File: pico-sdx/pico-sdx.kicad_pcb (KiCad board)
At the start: 2 copper layers, 76.7 x 64.5 mm, 100 parts, among them J1 AudioJack3, J2 AudioJack3, J3 Screw_Terminal_01x02, J4 Conn_Coaxial, J5 Conn_Coaxial, T1 T-622, T2 Transformer_SP_1S, U1 74HC74, U2 4066, U3 OPA2350, U4 LM321, U5 74HC74, U6 4066, U7 OPA1602, U8 uA7805, U9 uA7805

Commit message: update clock module footprint
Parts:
- moved J3 134.4 mm to (170.1, 92.3)
- moved C39 131.6 mm to (174.1, 77.9)
- moved C45 131.6 mm to (174.1, 82.9)
- moved C40 131.6 mm to (169.3, 66.3)
- moved C41 131.6 mm to (169.3, 69.5)
- moved C42 131.6 mm to (174.1, 80.4)
- moved C43 131.6 mm to (169.3, 72.6)
- moved C44 131.6 mm to (169.3, 75.8)
- moved U8 131.6 mm to (175.3, 68.7)
- moved U9 131.6 mm to (175.3, 74.6)
- moved C35 79.3 mm to (141.1, 28.5)
- moved R27 79.3 mm to (160.0, 28.4)
- moved R30 79.3 mm to (161.4, 23.0)
- moved RV2 79.3 mm to (174.4, 24.4)
- moved RV3 79.3 mm to (163.9, 19.4)
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
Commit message: add documentation and RaspberryPi Pico
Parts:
- added U11: RaspberryPi_Pico, Module_RaspberryPi_Pico:RaspberryPi_Pico_Common, F.Cu at (270.6, 101.0)
- C35, C36: moved to B.Cu
- C40: value 1µF -> 100nF; footprint Capacitor_Tantalum_SMD:CP_EIA-3216-18_Kemet-A -> Capacitor_SMD:C_0603_1608Metric
- C42: value 100nF -> 1µF; footprint Capacitor_SMD:C_0603_1608Metric -> Capacitor_Tantalum_SMD:CP_EIA-3216-18_Kemet-A
- moved C19 131.7 mm to (146.8, -16.0)
- moved C20 131.7 mm to (146.8, -17.5)
- moved R25 131.7 mm to (149.8, -19.0)
- moved R26 131.7 mm to (146.8, -19.0)
- moved R28 131.7 mm to (147.3, -21.6)
- moved R29 131.7 mm to (149.3, -21.6)
- moved C13 108.8 mm to (47.1, -32.0)
- moved C14 108.8 mm to (52.6, -31.0)
- moved C34 108.8 mm to (42.5, -29.9)
- moved R15 108.8 mm to (48.6, -32.0)
- moved R16 108.8 mm to (47.1, -28.9)
- moved U4 108.8 mm to (42.8, -32.8)
- moved C35 89.3 mm to (53.3, 45.0), turned to 0 degrees
- moved R27 82.6 mm to (92.0, -18.4)
- moved R30 82.6 mm to (93.4, -23.8)
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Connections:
- net /Oscillator/CLK0 renamed /downconverter/RX_LO
- net /Oscillator/CLK1 renamed /upconverter/TX_LO
- C41 pad 1: +5VA -> +12V
- C43 pad 1: +12V -> +5VD
- C44 pad 1: +5VD -> +5VA
- U10 pad 3: /Oscillator/CLK2 -> unconnected-(U10-CLK2-Pad3)
- U8 pad 3: +5VA -> +5VD
- U9 pad 3: +5VD -> +5VA
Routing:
- net +5VD: track 21.0 -> 25.2 mm
- net Net-(C24-Pad2): track 4.24 -> 2.27 mm
- net Net-(C21-Pad2): track 4.24 -> 2.52 mm

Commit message: routed with filter relays without PA
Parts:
- added C46: 1µF, Capacitor_SMD:C_0603_1608Metric, F.Cu at (101.9, 42.7)
- added C50: 1µF, Capacitor_SMD:C_0603_1608Metric, F.Cu at (101.9, 49.3)
- added D1: D, Diode_SMD:D_SOD-128, B.Cu at (28.8, 68.4)
- added D2: D, Diode_SMD:D_SOD-128, B.Cu at (104.7, 49.7)
- added D3: D, Diode_SMD:D_SOD-128, B.Cu at (28.7, 31.5)
- added D4: D, Diode_SMD:D_SOD-128, B.Cu at (41.7, 31.5)
- added D5: D, Diode_SMD:D_SOD-128, B.Cu at (54.7, 31.5)
- added D6: D, Diode_SMD:D_SOD-128, B.Cu at (67.7, 31.5)
- added D7: D, Diode_SMD:D_SOD-128, B.Cu at (80.7, 31.5)
- added D8: D, Diode_SMD:D_SOD-128, B.Cu at (93.7, 31.5)
- added D9: D, Diode_SMD:D_SOD-128, B.Cu at (107.2, 30.5)
- added J1: Antenna, Connector_Coaxial:SMA_Amphenol_132289_EdgeMount, F.Cu at (18.6, 77.9)
- added J2: RX, Connector_Coaxial:SMA_Amphenol_132289_EdgeMount, F.Cu at (18.6, 65.9)
- added J3: TX, Connector_Coaxial:SMA_Amphenol_132289_EdgeMount, F.Cu at (18.6, 89.9)
- added JP1: Jumper_3_Open, Connector_PinHeader_1.27mm:PinHeader_1x03_P1.27mm_Vertical, F.Cu at (24.2, 88.7)
- added JP2: Jumper_3_Open, Connector_PinHeader_1.27mm:PinHeader_1x03_P1.27mm_Vertical, F.Cu at (28.0, 88.7)
- added K1: G6K-2, Relay_THT:Relay_DPDT_Omron_G6K-2P, F.Cu at (108.0, 52.2)
- added K2: G6K-2, Relay_THT:Relay_DPDT_Omron_G6K-2P, F.Cu at (26.2, 71.7)
- added K3: G6K-2, Relay_THT:Relay_DPDT_Omron_G6K-2P, F.Cu at (25.9, 28.9)
- added K4: G6K-2, Relay_THT:Relay_DPDT_Omron_G6K-2P, F.Cu at (38.9, 28.9)
- added K5: G6K-2, Relay_THT:Relay_DPDT_Omron_G6K-2P, F.Cu at (51.9, 28.9)
- added K6: G6K-2, Relay_THT:Relay_DPDT_Omron_G6K-2P, F.Cu at (64.9, 28.9)
- added K7: G6K-2, Relay_THT:Relay_DPDT_Omron_G6K-2P, F.Cu at (77.9, 28.9)
- added K8: G6K-2, Relay_THT:Relay_DPDT_Omron_G6K-2P, F.Cu at (90.9, 28.9)
- added K9: G6K-2, Relay_THT:Relay_DPDT_Omron_G6K-2P, F.Cu at (103.9, 28.9)
- added L1: 27µH, Inductor_SMD:L_Bourns_SRR1208_12.7x12.7mm, F.Cu at (93.8, 46.0)
- added R36: 1.8R, Resistor_SMD:R_0603_1608Metric, F.Cu at (101.2, 40.4)
- added TP1: RX_LO, TestPoint:TestPoint_Loop_D1.80mm_Drill1.0mm_Beaded, F.Cu at (125.2, 49.9)
- added TP10: TestPoint, TestPoint:TestPoint_Loop_D1.80mm_Drill1.0mm_Beaded, F.Cu at (167.1, 46.4)
- added TP11: TestPoint, TestPoint:TestPoint_Loop_D1.80mm_Drill1.0mm_Beaded, F.Cu at (148.2, 36.9)
- added TP12: TestPoint, TestPoint:TestPoint_Loop_D1.80mm_Drill1.0mm_Beaded, F.Cu at (140.2, 48.7)
- added TP2: TX_LO, TestPoint:TestPoint_Loop_D1.80mm_Drill1.0mm_Beaded, F.Cu at (129.2, 48.9)
- added TP3: RX_TR_Midpoint, TestPoint:TestPoint_Loop_D1.80mm_Drill1.0mm_Beaded, F.Cu at (112.2, 76.9)
- added TP4: RX_OPAMP_Midpoint, TestPoint:TestPoint_Loop_D1.80mm_Drill1.0mm_Beaded, F.Cu at (144.8, 63.8)
- added TP5: TestPoint, TestPoint:TestPoint_Loop_D1.80mm_Drill1.0mm_Beaded, F.Cu at (152.1, 36.7)
- added TP6: TestPoint, TestPoint:TestPoint_Loop_D1.80mm_Drill1.0mm_Beaded, F.Cu at (147.4, 22.6)
- added TP7: TestPoint, TestPoint:TestPoint_Loop_D1.80mm_Drill1.0mm_Beaded, F.Cu at (167.1, 62.7)
- added TP8: TestPoint, TestPoint:TestPoint_Loop_D1.80mm_Drill1.0mm_Beaded, F.Cu at (135.6, 39.5)
- added TP9: TestPoint, TestPoint:TestPoint_Loop_D1.80mm_Drill1.0mm_Beaded, F.Cu at (139.7, 39.5)
- added U1: MAX4820xUP, Package_SO:HTSSOP-20-1EP_4.4x6.5mm_P0.65mm_EP2.85x4mm, B.Cu at (94.5, 66.9)
- added U13: HMC589A, Package_TO_SOT_SMD:SOT-89-3, F.Cu at (103.3, 46.0)
- added X1: 40 m, pico-sdx:Filter Module, F.Cu at (22.2, 40.9)
- added X2: 30 m, pico-sdx:Filter Module, F.Cu at (35.2, 40.9)
- added X3: 20 m, pico-sdx:Filter Module, F.Cu at (48.2, 40.9)
- added X4: 17 m, pico-sdx:Filter Module, F.Cu at (61.2, 40.9)
- added X5: 15 m, pico-sdx:Filter Module, F.Cu at (74.2, 40.9)
- added X6: 12 m, pico-sdx:Filter Module, F.Cu at (87.2, 40.9)
- added X7: 10 m, pico-sdx:Filter Module, F.Cu at (100.2, 40.9)
- C14: renamed from C36; moved to F.Cu
- C42: renamed from C35; moved to F.Cu
- J4, J5: footprint Connector_Coaxial:SMA_Amphenol_132289_EdgeMount -> Connector_Coaxial:SMA_Amphenol_132291_Vertical
- J8: renamed from J3; value Screw_Terminal_01x02 -> Barrel_Jack_Switch; footprint TerminalBlock:TerminalBlock_Wuerth_691311400102_P7.62mm -> Connector_BarrelJack:BarrelJack_Wuerth_6941xx301002
- U6: renamed from U1; moved to F.Cu
- U9: renamed from U5; moved to F.Cu
- moved C22 127.6 mm to (155.2, 63.4), turned to 90 degrees
- moved C19 126.4 mm to (149.2, 64.8)
- moved R13 126.4 mm to (149.2, 61.5)
- moved R14 126.4 mm to (147.5, 64.8)
- moved C31 125.6 mm to (154.7, 42.3)
- moved C32 125.6 mm to (149.1, 41.4)
- moved C38 125.6 mm to (144.5, 43.4)
- moved R25 125.6 mm to (149.1, 44.4)
- moved R26 125.6 mm to (150.6, 41.4)
- moved U11 125.6 mm to (144.8, 40.5)
- moved J8 122.1 mm to (29.6, 100.7), turned to -90 degrees
- moved U2 121.7 mm to (149.1, 95.1), turned to -90 degrees
- moved RV2 113.2 mm to (170.6, 57.7)
- moved R29 111.6 mm to (168.1, 59.0)
- moved R33 105.4 mm to (168.1, 54.5)
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- renumbered C39 to C1, C4 to C10, C3 to C11, C5 to C12, C6 to C13, C7 to C15, C8 to C16, C37 to C17, C9 to C18, C11 to C19, C40 to C2, C38 to C20, C10 to C21, C12 to C22, C15 to C23, C16 to C24, C17 to C25, C18 to C26, C21 to C27, C22 to C28, C23 to C29, C41 to C3, C24 to C30, C14 to C31, C13 to C32, C25 to C33, C26 to C34, C27 to C35, C28 to C36, C31 to C37, C34 to C38, C30 to C39, C42 to C4, C33 to C40, C29 to C41, C20 to C43, C32 to C44, C19 to C45, C43 to C5, C44 to C6, C45 to C7, C1 to C8, C2 to C9, J1 to J6, J2 to J7, R17 to R15, R18 to R16, R21 to R17, R22 to R18, R20 to R19, R19 to R20, R32 to R21, R33 to R22, R34 to R23, R35 to R24, R16 to R25, R15 to R26, R23 to R27, R24 to R28, R30 to R29, R28 to R30, R25 to R31, R26 to R32, R27 to R33, R29 to R34, R31 to R35, R6 to R5, R5 to R6, RV3 to RV2, RV2 to RV3, U7 to U10, U4 to U11, U6 to U12, U11 to U2, U10 to U3, U8 to U4, U9 to U5, U2 to U7, U3 to U8
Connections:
- net /downconverter/2.5V_OPAMP renamed /Downconverter/2.5V_OPAMP
- net /downconverter/2.5V_TR renamed /Downconverter/2.5V_TR
- net /downconverter/CLK_I renamed /Downconverter/CLK_I
- net /downconverter/CLK_Q renamed /Downconverter/CLK_Q
- net /downconverter/RX_I renamed /Downconverter/RX_I
- net /downconverter/RX_IN renamed /Downconverter/RX_IN
- net /downconverter/RX_Q renamed /Downconverter/RX_Q
- net /downconverter/~{CLK_I} renamed /Downconverter/~{CLK_I}
- net /downconverter/~{CLK_Q} renamed /Downconverter/~{CLK_Q}
- net /upconverter/2.5V renamed /Upconverter/2.5V
- net /upconverter/BIAS renamed /Upconverter/BIAS
- net /upconverter/BIAS_I renamed /Upconverter/BIAS_I
- net /upconverter/BIAS_Q renamed /Upconverter/BIAS_Q
- net /upconverter/CLK_I renamed /Upconverter/CLK_I
- net /upconverter/CLK_Q renamed /Upconverter/CLK_Q
- net /upconverter/TX_I renamed /Upconverter/TX_I
- net /upconverter/TX_OUT renamed /Upconverter/TX_OUT
- net /upconverter/TX_Q renamed /Upconverter/TX_Q
- net /upconverter/~{BIAS_I} renamed /Upconverter/~{BIAS_I}
- net /upconverter/~{BIAS_Q} renamed /Upconverter/~{BIAS_Q}
- net /upconverter/~{CLK_I} renamed /Upconverter/~{CLK_I}
- net /upconverter/~{CLK_Q} renamed /Upconverter/~{CLK_Q}
- R33 pad 2: Net-(R27-Pad2) (its old number) -> Net-(R33-Pad2)
- RV2 pad 1: GND -> Net-(R33-Pad2)
- RV2 pad 3: Net-(R27-Pad2) (its old number) -> GND
- RV3 pad 1: Net-(R27-Pad2) (its old number) -> GND
- RV3 pad 3: GND -> Net-(R33-Pad2)
- U2 pad 19: unconnected-(U11-GPIO14-Pad19) -> SDA
- U2 pad 20: unconnected-(U11-GPIO15-Pad20) -> SCL
- U2 pad 21: unconnected-(U11-GPIO16-Pad21) -> MISO
- U2 pad 22: unconnected-(U11-GPIO17-Pad22) -> ~{CS}
- U2 pad 24: unconnected-(U11-GPIO18-Pad24) -> SCLK
- U2 pad 25: SDA -> MOSI
- U2 pad 26: SCL -> ~{RESET}
- U2 pad 39: unconnected-(U11-VSYS-Pad39) -> +5VD
- U3 pad 1: /downconverter/RX_LO -> +5VD
- U3 pad 2: /upconverter/TX_LO -> GND
- U3 pad 3: unconnected-(U10-CLK2-Pad3) -> SDA
- U3 pad 5: SDA -> unconnected-(U3-CLK2-Pad5)
- U3 pad 6: GND -> RX_LO
- U3 pad 7: (no net) -> TX_LO
- U6 pad 11: /downconverter/RX_LO -> RX_LO
- U6 pad 3: /downconverter/RX_LO -> RX_LO
- U9 pad 11: /upconverter/TX_LO -> TX_LO
- U9 pad 3: /upconverter/TX_LO -> TX_LO
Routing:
- net +5VD: track 25.2 -> 304.7 mm, vias 0 -> 6
- net +5VA: track 5.15 -> 263.4 mm, vias 0 -> 8
- net /Bandpass Filter/RF in: track 0.00 -> 123.2 mm
- net /Bandpass Filter/RF out: track 0.00 -> 122.7 mm
- net /PA/TX in: track 0.00 -> 119.4 mm
- net Net-(J2-In): track 0.00 -> 113.2 mm
- net +12V: track 0.00 -> 112.3 mm
- net TX~{RX}: track 0.00 -> 110.7 mm, vias 0 -> 2
- net 40 m: track 0.00 -> 102.2 mm
- net 30 m: track 0.00 -> 89.7 mm
- net 20 m: track 0.00 -> 76.4 mm
- net ~{RESET}: track 0.00 -> 75.1 mm
- net MOSI: track 0.00 -> 73.7 mm
- net SCLK: track 0.00 -> 71.8 mm
- net ~{CS}: track 0.00 -> 66.4 mm, vias 0 -> 1
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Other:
- board size 76.7 x 64.5 mm -> 160 x 100 mm
- board text added: "{ "ViaStitching": "0.2", "stitch_zone_0": { "HSpacing": "1", "VSpacing": "1", "Clearance": "0.2", "Randomize": false } }"

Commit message: add active lowpass filter in upconverter branch
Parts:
- added C51: 100nF, Capacitor_SMD:C_0603_1608Metric, F.Cu at (140.7, 26.8)
- added C52: 100pF, Capacitor_SMD:C_1206_3216Metric, F.Cu at (151.4, 34.5)
- added C53: 100pF, Capacitor_SMD:C_1206_3216Metric, F.Cu at (151.4, 26.6)
- added R37: 10k, Resistor_SMD:R_0603_1608Metric, F.Cu at (153.4, 25.8)
- added R38: 10k, Resistor_SMD:R_0603_1608Metric, F.Cu at (153.4, 32.4)
- added R39: 7.5k, Resistor_SMD:R_0603_1608Metric, F.Cu at (153.4, 29.1)
- added R40: 7.5k, Resistor_SMD:R_0603_1608Metric, F.Cu at (153.4, 22.5)
- added U14: OPA1602, Package_SO:SOIC-8_3.9x4.9mm_P1.27mm, F.Cu at (146.3, 25.2)
- moved TP6 24.3 mm to (164.8, 39.5)
- moved C44 12.3 mm to (143.2, 35.9), turned to 180 degrees
- moved TP5 8.12 mm to (159.7, 39.5)
- moved R16 7.97 mm to (158.5, 21.5)
- moved C25 7.88 mm to (156.7, 34.7), turned to 180 degrees
- moved C26 7.19 mm to (155.4, 23.0), turned to 90 degrees
- moved R18 5.21 mm to (146.8, 21.6), turned to 180 degrees
- moved U10 4.61 mm to (146.3, 32.3), turned to 180 degrees
- moved R15 4.44 mm to (158.5, 32.7)
- moved C23 4.06 mm to (155.9, 31.4)
- moved C24 4.06 mm to (155.9, 27.3)
- moved R17 3.18 mm to (146.8, 28.7), turned to 180 degrees
- moved C29 2.84 mm to (139.4, 28.9), turned to 180 degrees
- moved R19 2.16 mm to (141.7, 32.3), turned to -90 degrees
- moved R20 1.61 mm to (141.6, 24.0), turned to -90 degrees
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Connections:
- C27 pad 1: Net-(C25-Pad2) -> Net-(C27-Pad1)
- C29 pad 1: Net-(C26-Pad2) -> Net-(C29-Pad1)
- R17 pad 1: Net-(C25-Pad2) -> Net-(C27-Pad1)
- R17 pad 2: Net-(U10A--) -> Net-(U10B--)
- R18 pad 1: Net-(C26-Pad2) -> Net-(C29-Pad1)
- R18 pad 2: Net-(U10B--) -> Net-(U14B--)
- R19 pad 1: Net-(U10A--) -> Net-(U10B--)
- R20 pad 1: Net-(U10B--) -> Net-(U14B--)
- U10 pad 1: Net-(C28-Pad1) -> Net-(C27-Pad1)
- U10 pad 7: Net-(C30-Pad1) -> Net-(C28-Pad1)
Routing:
- net /Upconverter/2.5V: track 24.5 -> 53.2 mm, vias 2 -> 4
- net Net-(C27-Pad1): track 0.00 -> 25.7 mm
- net Net-(C29-Pad1): track 0.00 -> 20.6 mm
- net Net-(C24-Pad1): track 9.13 -> 26.0 mm, vias 0 -> 1
- net Net-(C26-Pad2): track 12.4 -> 2.09 mm
- net Net-(C25-Pad2): track 17.2 -> 7.14 mm
- net GND: track 50.9 -> 60.6 mm, vias 24 -> 17
- net Net-(U14B--): track 0.00 -> 7.10 mm
- net Net-(U14A--): track 0.00 -> 6.63 mm
- net /Upconverter/~{BIAS_Q}: track 56.2 -> 62.6 mm
- net Net-(C30-Pad1): track 12.0 -> 6.56 mm
- net /Upconverter/TX_Q: track 18.3 -> 13.0 mm
- net Net-(R15-Pad1): track 20.8 -> 16.0 mm
- net +5VA: track 263.4 -> 265.8 mm, vias 8 -> 9
- net Net-(C29-Pad2): track 4.37 -> 2.62 mm
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
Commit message: modular design
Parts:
- removed D1, D2, D3, D4, D5, D6, D7, D8, D9: D, Diode_SMD:D_SOD-128
- removed J1: Antenna, Connector_Coaxial:SMA_Amphenol_132289_EdgeMount
- removed J2: RX, Connector_Coaxial:SMA_Amphenol_132289_EdgeMount
- removed J3: TX, Connector_Coaxial:SMA_Amphenol_132289_EdgeMount
- removed JP1, JP2: Jumper_3_Open, Connector_PinHeader_1.27mm:PinHeader_1x03_P1.27mm_Vertical
- removed K1, K2, K3, K4, K5, K6, K7, K8, K9: G6K-2, Relay_THT:Relay_DPDT_Omron_G6K-2P
- removed TP1: RX_LO, TestPoint:TestPoint_Loop_D1.80mm_Drill1.0mm_Beaded
- removed TP2: TX_LO, TestPoint:TestPoint_Loop_D1.80mm_Drill1.0mm_Beaded
- removed U1: MAX4820xUP, Package_SO:HTSSOP-20-1EP_4.4x6.5mm_P0.65mm_EP2.85x4mm
- removed U2: RaspberryPi_Pico, Module_RaspberryPi_Pico:RaspberryPi_Pico_Common
- removed U4: uA7805, Package_TO_SOT_THT:TO-220-3_Vertical
- removed X1: 40 m, pico-sdx:Filter Module
- removed X2: 30 m, pico-sdx:Filter Module
- removed X3: 20 m, pico-sdx:Filter Module
- removed X4: 17 m, pico-sdx:Filter Module
- removed X5: 15 m, pico-sdx:Filter Module
- removed X6: 12 m, pico-sdx:Filter Module
- removed X7: 10 m, pico-sdx:Filter Module
- added PMOD1: PMOD-Device-x2-Type-2A-Expanded-SPI, pmod-conn_6x2:pmod_pin_array_6x2, F.Cu at (40.0, 72.3)
- added U17: TLE4284 DV33, Package_TO_SOT_SMD:TO-252-3_TabPin2, F.Cu at (92.3, 88.7)
- added X8: TCXO-14, Oscillator:Oscillator_DIP-14, F.Cu at (121.2, 59.7)
- U3: value ~ -> Si5351C-B-GU; footprint pico-sdx:Module_Si5351 -> Package_SO:QSOP-24_3.9x8.7mm_P0.635mm
- moved J8 52.8 mm to (67.6, 64.1)
- moved C1 44.0 mm to (86.6, 70.7)
- moved C3 44.0 mm to (85.8, 72.7)
- moved C5 44.0 mm to (91.9, 72.7)
- moved C7 44.0 mm to (91.1, 70.7)
- moved C2 36.9 mm to (88.2, 55.9)
- moved C6 36.9 mm to (93.5, 56.2)
- moved C4 36.8 mm to (87.5, 58.0)
- moved U5 36.8 mm to (88.0, 53.4)
- moved C14 36.6 mm to (121.5, 89.7)
- moved C10 33.4 mm to (132.8, 108.5)
- moved C11 33.4 mm to (129.2, 108.5)
- moved C12 33.4 mm to (144.4, 102.4)
- moved C15 33.4 mm to (148.0, 102.4)
- moved C17 33.4 mm to (135.8, 109.0)
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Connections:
- C14 pad 1: +5VD -> +3.3V
- C17 pad 1: +5VD -> +3.3V
- C40 pad 1: +5VD -> +3.3V
- C42 pad 1: +5VD -> +3.3V
- C46 pad 1: /Bandpass Filter/RF out -> /Buffer Amplifier/RF in
- C5 pad 1: +5VD -> +3.3V
- C7 pad 1: +5VD -> +3.3V
- J4 pad 1: /Downconverter/RX_IN -> /Buffer Amplifier/RF in
- T1 pad 1: /Downconverter/RX_IN -> /Buffer Amplifier/RF out
- U12 pad 14: +5VD -> +3.3V
- U3 pad 1: +5VD -> unconnected-(U3-CLK5-Pad1)
- U3 pad 2: GND -> +3.3V
- U3 pad 3: SDA -> unconnected-(U3-CLK4-Pad3)
- U3 pad 4: SCL -> +3.3V
- U3 pad 5: unconnected-(U3-CLK2-Pad5) -> GND
- U3 pad 6: RX_LO -> unconnected-(U3-XA-Pad6)
- U3 pad 7: TX_LO -> unconnected-(U3-XB-Pad7)
- U6 pad 1: +5VD -> +3.3V
- U6 pad 10: +5VD -> +3.3V
- U6 pad 13: +5VD -> +3.3V
- U6 pad 14: +5VD -> +3.3V
- U6 pad 4: +5VD -> +3.3V
- U7 pad 14: +5VD -> +3.3V
- U9 pad 1: +5VD -> +3.3V
- U9 pad 10: +5VD -> +3.3V
- U9 pad 13: +5VD -> +3.3V
- U9 pad 14: +5VD -> +3.3V
- U9 pad 4: +5VD -> +3.3V
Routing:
- net +5VD: track 304.7 -> 0.00 mm, vias 6 -> 0
- net +5VA: track 265.8 -> 0.00 mm, vias 9 -> 0
- net /Bandpass Filter/RF in: track 123.2 -> 0.00 mm
- net /Bandpass Filter/RF out: track 122.7 -> 0.00 mm
- net /PA/TX in: track 119.4 -> 0.00 mm
- net Net-(J2-In): track 113.2 -> 0.00 mm
- net TX~{RX}: track 110.7 -> 0.00 mm, vias 2 -> 0
- net 40 m: track 102.2 -> 0.00 mm
- net +12V: track 112.3 -> 11.6 mm
- net 30 m: track 89.7 -> 0.00 mm
- net 20 m: track 76.4 -> 0.00 mm
- net ~{RESET}: track 75.1 -> 0.00 mm
- net MOSI: track 73.7 -> 0.00 mm
- net SCLK: track 71.8 -> 0.00 mm
- net ~{CS}: track 66.4 -> 0.00 mm, vias 1 -> 0
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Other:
- board size 160 x 100 mm -> 100 x 100 mm

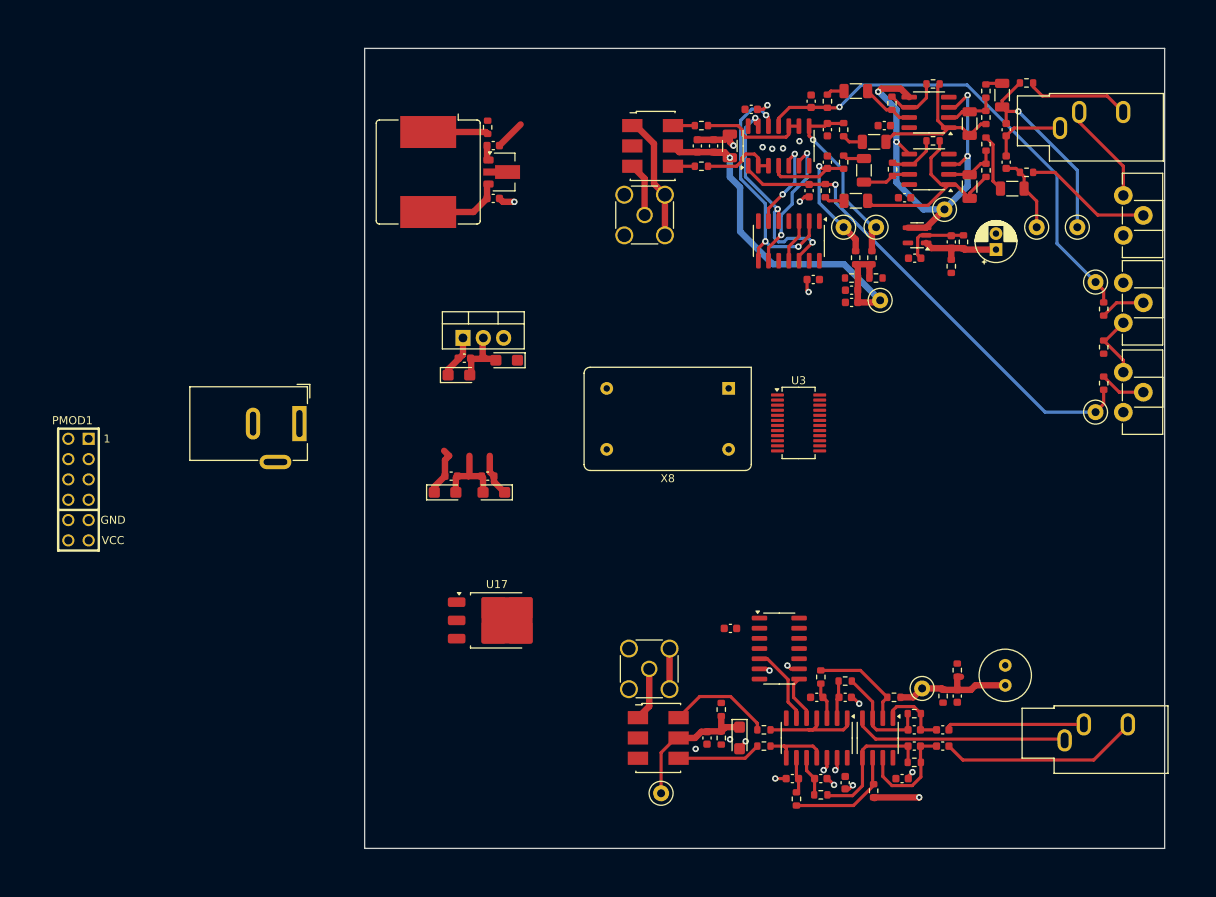
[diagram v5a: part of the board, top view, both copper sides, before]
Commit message: mixer routed
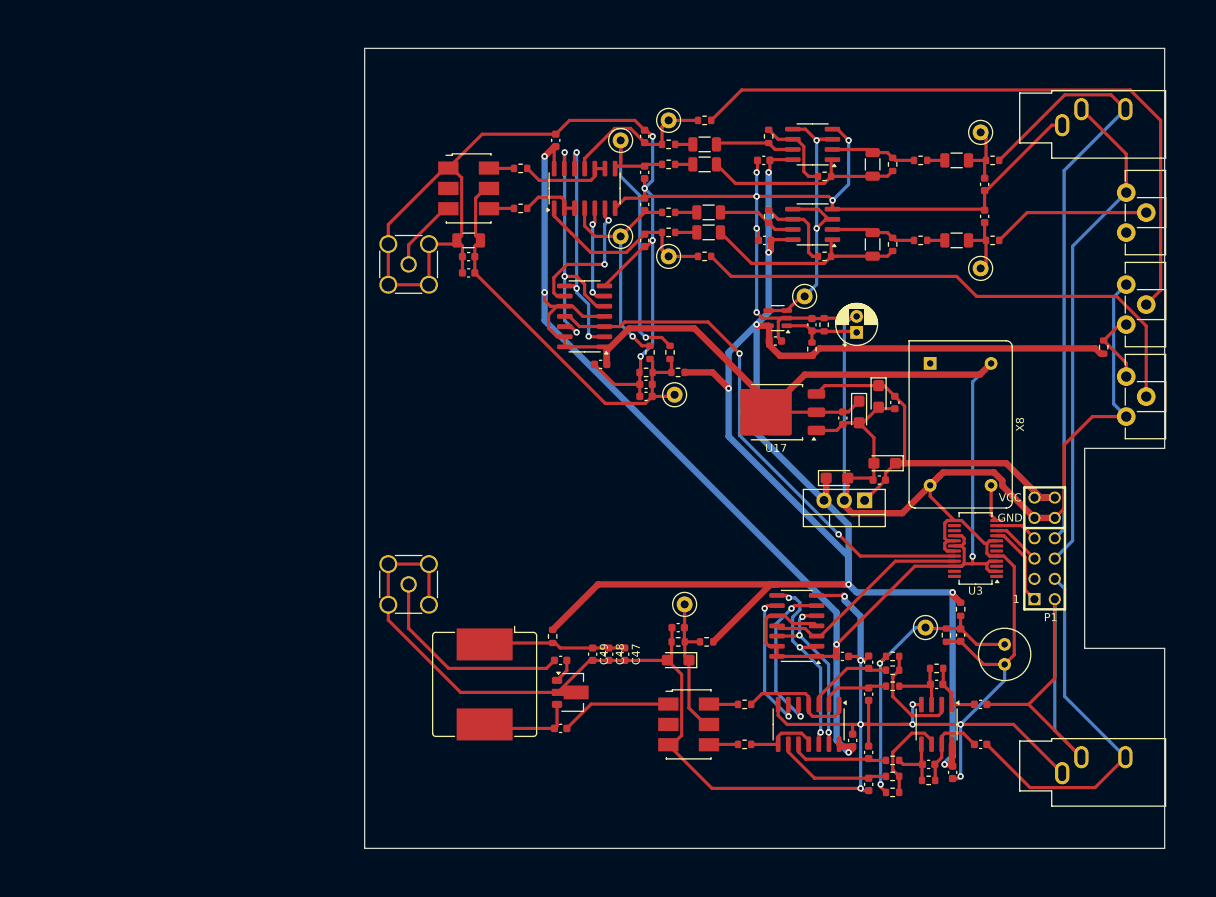
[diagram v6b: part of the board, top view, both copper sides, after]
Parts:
- removed J8: Barrel_Jack_Switch, Connector_BarrelJack:BarrelJack_Wuerth_6941xx301002
- removed PMOD1: PMOD-Device-x2-Type-2A-Expanded-SPI, pmod-conn_6x2:pmod_pin_array_6x2
- added C47: 2.2µF, Capacitor_SMD:C_0603_1608Metric, F.Cu at (108.2, 92.9)
- added C48: 1000pF, Capacitor_SMD:C_0603_1608Metric, F.Cu at (106.2, 92.9)
- added C49: 100pF, Capacitor_SMD:C_0603_1608Metric, F.Cu at (104.2, 92.9)
- added P1: PMOD-Device-x2-Type-Generic-Alt, pmod-conn_6x2:pmod_pin_array_6x2, F.Cu at (160.7, 79.7)
- moved C50 66.8 mm to (100.2, 102.2)
- moved U13 65.6 mm to (101.7, 97.7)
- moved C46 64.9 mm to (100.2, 93.7), turned to 0 degrees
- moved L1 64.4 mm to (90.7, 96.7)
- moved R36 64.2 mm to (99.2, 90.7)
- moved TP10 57.1 mm to (113.7, 26.2)
- moved TP7 56.8 mm to (113.7, 43.2)
- moved C1 56.2 mm to (142.0, 61.4), turned to -90 degrees
- moved C3 55.5 mm to (140.0, 60.7), turned to -90 degrees
- moved R35 55.2 mm to (118.2, 26.2), turned to 180 degrees
- moved C4 54.4 mm to (140.7, 69.0), turned to 180 degrees
- moved U5 54.2 mm to (138.2, 73.7), turned to 180 degrees
- moved C2 54.1 mm to (140.1, 71.1), turned to 180 degrees
- moved R29 52.3 mm to (118.2, 43.2), turned to 0 degrees
- moved C5 46.7 mm to (137.5, 62.6), turned to -90 degrees
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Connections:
- net /Downconverter/RX_I renamed RX_I
- net /Downconverter/RX_Q renamed RX_Q
- net /Upconverter/TX_I renamed TX_I
- net /Upconverter/TX_Q renamed TX_Q
- U3 pad 11: (no net) -> SDA
- U3 pad 9: unconnected-(U3-INTR-Pad9) -> INT
- U6 pad 12: /Downconverter/~{CLK_Q} -> /Downconverter/CLK_I
- U6 pad 2: /Downconverter/CLK_I -> /Downconverter/~{CLK_Q}
- U6 pad 5: /Downconverter/CLK_Q -> /Downconverter/CLK_I
- U6 pad 6: /Downconverter/~{CLK_Q} -> /Downconverter/~{CLK_I}
- U6 pad 8: /Downconverter/~{CLK_I} -> /Downconverter/~{CLK_Q}
- U6 pad 9: /Downconverter/CLK_I -> /Downconverter/CLK_Q
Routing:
- net GND: track 101.7 -> 610.2 mm, vias 16 -> 18
- net +3.3V: track 5.34 -> 273.1 mm, vias 0 -> 5
- net +5VA: track 0.00 -> 253.3 mm, vias 0 -> 7
- net Net-(R35-Pad1): track 5.62 -> 83.1 mm
- net TX_Q: track 13.0 -> 77.2 mm
- net TX_LO: track 5.48 -> 67.6 mm, vias 0 -> 2
- net Net-(R29-Pad2): track 5.77 -> 66.8 mm
- net TX_I: track 12.7 -> 62.2 mm
- net /Upconverter/~{BIAS_Q}: track 62.6 -> 20.3 mm, vias 1 -> 0
- net +12V: track 11.6 -> 50.9 mm
- net /Upconverter/BIAS_I: track 63.3 -> 24.4 mm, vias 1 -> 0
- net RX_I: track 17.4 -> 50.2 mm
- net RX_LO: track 0.00 -> 26.6 mm
- net /Buffer Amplifier/RF in: track 3.75 -> 26.2 mm
- net RX_Q: track 24.8 -> 47.1 mm
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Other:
- outline, holes or cut-outs redrawn

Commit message: clean up
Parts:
- moved TP11 0.50 mm to (130.7, 47.7)
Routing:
- net +3.3V: track 273.1 -> 275.3 mm
- net /Upconverter/2.5V: track 40.8 -> 42.6 mm
- net Net-(U8B--): track 12.0 -> 12.9 mm
- net Net-(U8A--): track 13.6 -> 14.5 mm
- net GND: track 610.2 -> 610.7 mm, vias 18 -> 2281
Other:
- board text added: "pico SDX Tayloe mixer by Hannes"
